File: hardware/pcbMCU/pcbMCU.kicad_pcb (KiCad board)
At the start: 2 copper layers, 53 parts, among them J1 Conn_01x02, J2 Conn_01x04, J3 Conn_01x03, J4 Conn_01x05, SW1 SW_SPDT, U1 AMS1117-3.3, U2 AP62300, U3 STM32L412Cx, U4 Ai-Thinker-Ra-02, U5 RFM95W-915S2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

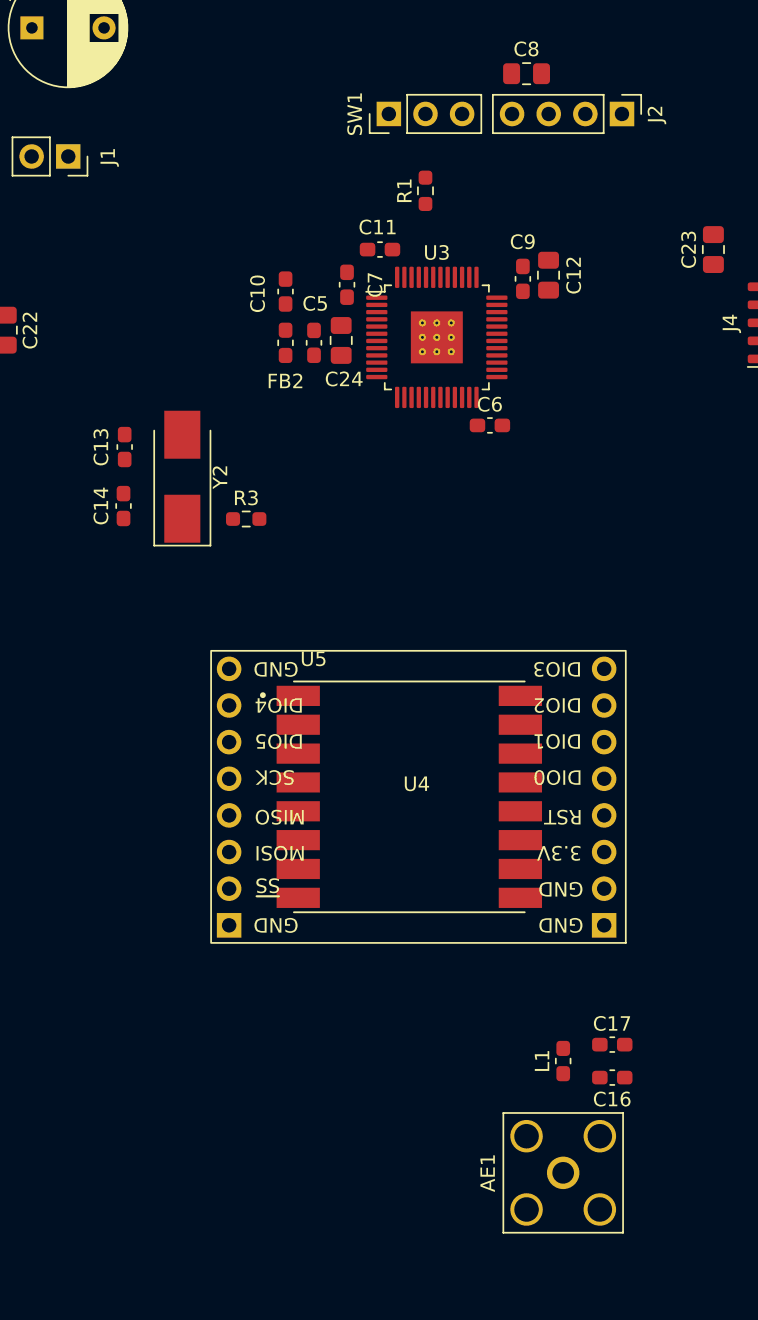
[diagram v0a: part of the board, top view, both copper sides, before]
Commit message: Cambio a ESP32
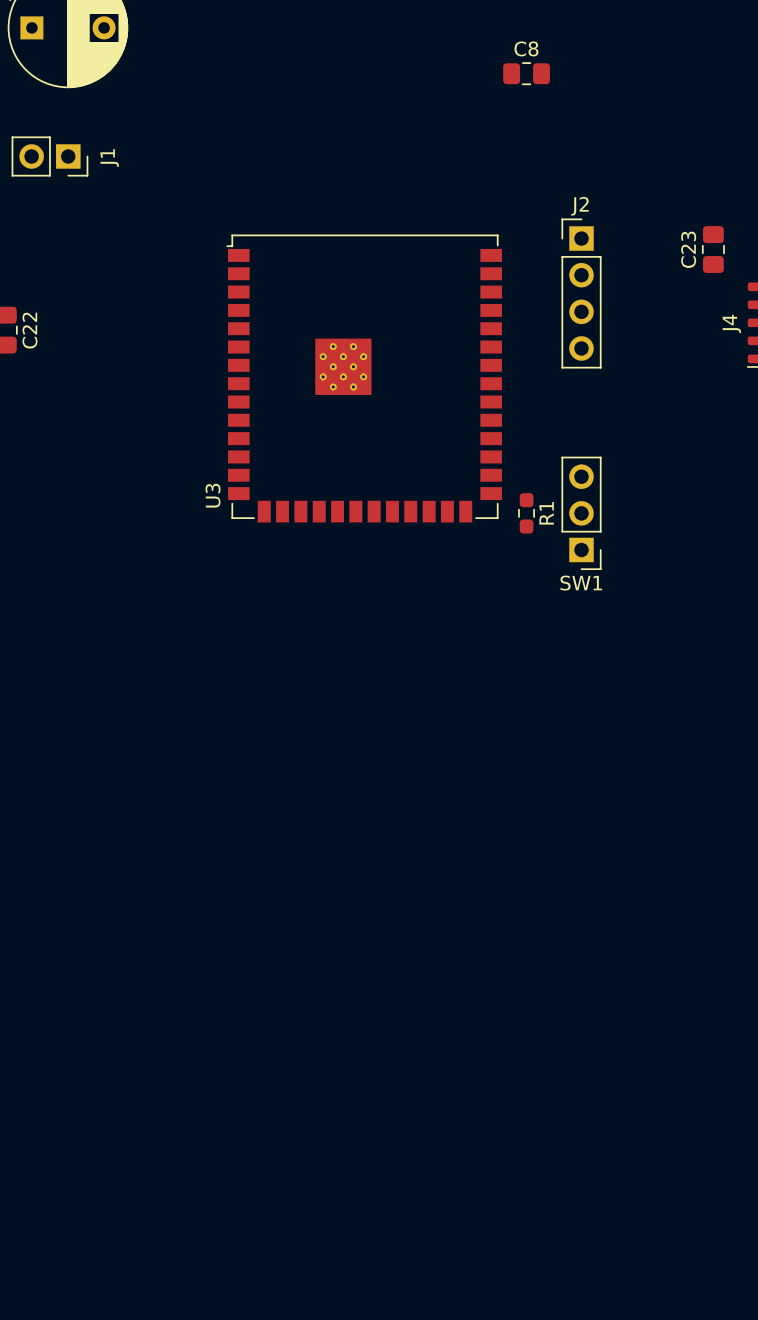
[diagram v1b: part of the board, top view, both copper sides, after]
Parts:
- removed AE1: Antenna_Shield, Connector_Coaxial:SMA_Amphenol_132203-12_Horizontal
- removed C10, C11, C5, C6, C7, C9: 100n, Capacitor_SMD:C_0603_1608Metric_Pad1.08x0.95mm_HandSolder
- removed C12: 4u7, Capacitor_SMD:C_0805_2012Metric_Pad1.18x1.45mm_HandSolder
- removed C13, C14: 10p, Capacitor_SMD:C_0603_1608Metric_Pad1.08x0.95mm_HandSolder
- removed C16, C17: DNP, Capacitor_SMD:C_0603_1608Metric_Pad1.08x0.95mm_HandSolder
- removed C24: 1u, Capacitor_SMD:C_0805_2012Metric_Pad1.18x1.45mm_HandSolder
- removed FB2: 100 @ 100MHz, Inductor_SMD:L_0603_1608Metric_Pad1.05x0.95mm_HandSolder
- removed L1: 0, Inductor_SMD:L_0603_1608Metric_Pad1.05x0.95mm_HandSolder
- removed R3: 0, Resistor_SMD:R_0603_1608Metric_Pad0.98x0.95mm_HandSolder
- removed U4: Ai-Thinker-Ra-02, RF_Module:Ai-Thinker-Ra-02-LoRa-THT
- removed U5: RFM95W-915S2, pcbMCU:XCVR_RFM95W-915S2
- removed Y2: 8MHz, Crystal:Crystal_SMD_0603-2Pin_6.0x3.5mm_HandSoldering
- U3: value STM32L412Cx -> ESP32-S3-WROOM-1; footprint Package_QFP:LQFP-48-1EP_7x7mm_P0.5mm_EP3.6x3.6mm_ThermalVias -> RF_Module:ESP32-S3-WROOM-1U
- moved SW1 33.0 mm to (77.5, 76.2), turned to 180 degrees
- moved R1 23.4 mm to (73.7, 73.7), turned to -90 degrees
- moved J2 9.08 mm to (77.5, 54.6), turned to 0 degrees
- moved U3 5.68 mm to (62.5, 64.2)
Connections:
- net SWDCLK renamed UART_RX
- J2 pad 3: SWDIO -> UART_TX
- U3 pad 1: +3V3 -> GND
- U3 pad 10: ADC_MIC -> unconnected-(U3-Pad10)
- U3 pad 11: ADC_SP -> unconnected-(U3-Pad11)
- U3 pad 15: SPI1_SCK -> unconnected-(U3-Pad15)
- U3 pad 16: SPI1_MISO -> unconnected-(U3-Pad16)
- U3 pad 17: SPI1_MOSI -> unconnected-(U3-Pad17)
- U3 pad 18: ~{SS} -> unconnected-(U3-Pad18)
- U3 pad 19: LoRa_~{RST} -> unconnected-(U3-Pad19)
- U3 pad 2: unconnected-(U3-Pad2) -> +3V3
- U3 pad 20: LoRa_DIO0 -> unconnected-(U3-Pad20)
- U3 pad 23: GND -> unconnected-(U3-Pad23)
- U3 pad 24: +3V3 -> unconnected-(U3-Pad24)
- U3 pad 27: unconnected-(U3-Pad27) -> BOOT0
- U3 pad 3: LS_OSCIN -> unconnected-(U3-Pad3)
- U3 pad 30: SCL_SP -> unconnected-(U3-Pad30)
- U3 pad 31: SDA_SP -> unconnected-(U3-Pad31)
- U3 pad 34: SWDIO -> unconnected-(U3-Pad34)
- U3 pad 35: GND -> unconnected-(U3-Pad35)
- U3 pad 36: +3V3 -> UART_TX
- U3 pad 4: LS_OSCOUT -> unconnected-(U3-Pad4)
- U3 pad 40: unconnected-(U3-Pad40) -> GND
- U3 pad 41: unconnected-(U3-Pad41) -> GND
- U3 pad 5: HS_OSCIN -> unconnected-(U3-Pad5)
- U3 pad 6: HS_OSCOUT -> unconnected-(U3-Pad6)
- U3 pad 7: ~{RST} -> unconnected-(U3-Pad7)
- U3 pad 8: GND -> unconnected-(U3-Pad8)
- U3 pad 9: +3.3VA -> unconnected-(U3-Pad9)

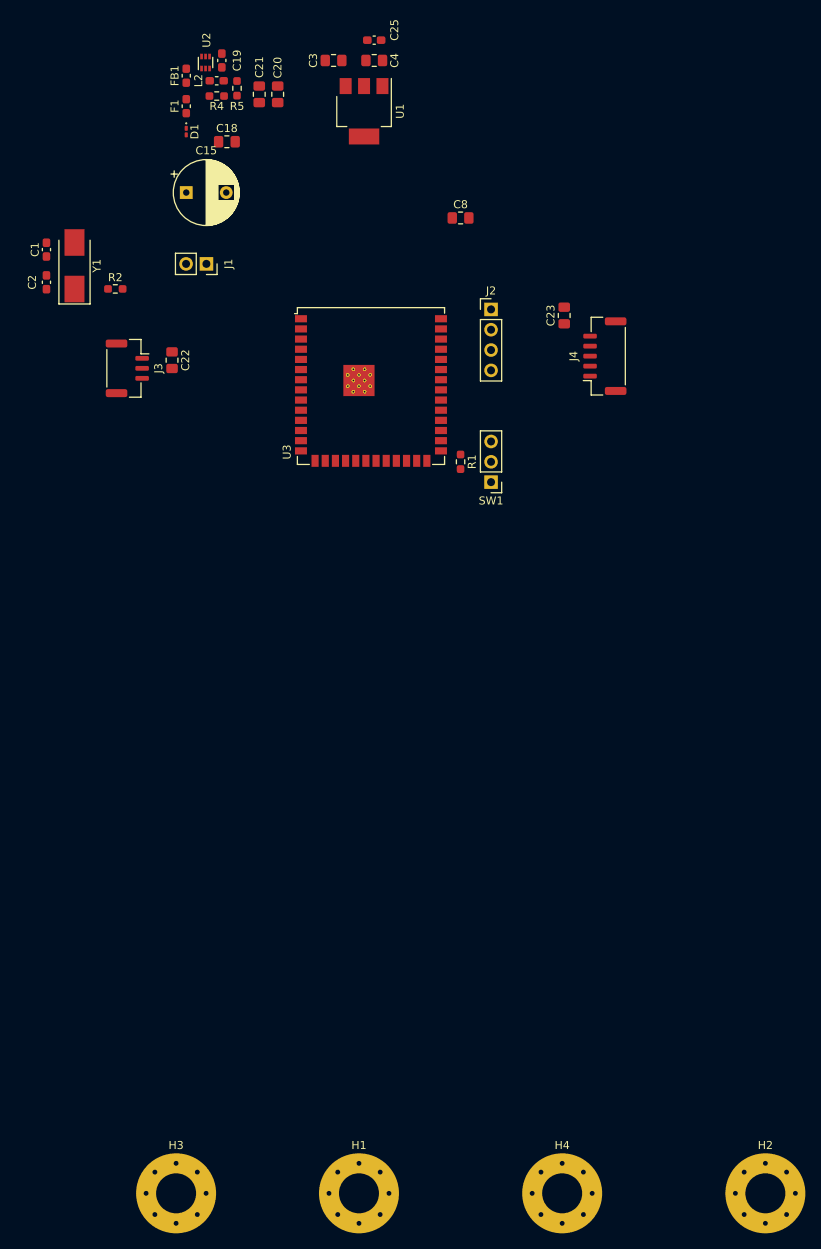
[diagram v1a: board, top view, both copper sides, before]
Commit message: Esquema de PCB inicial, agrupación general de componentes
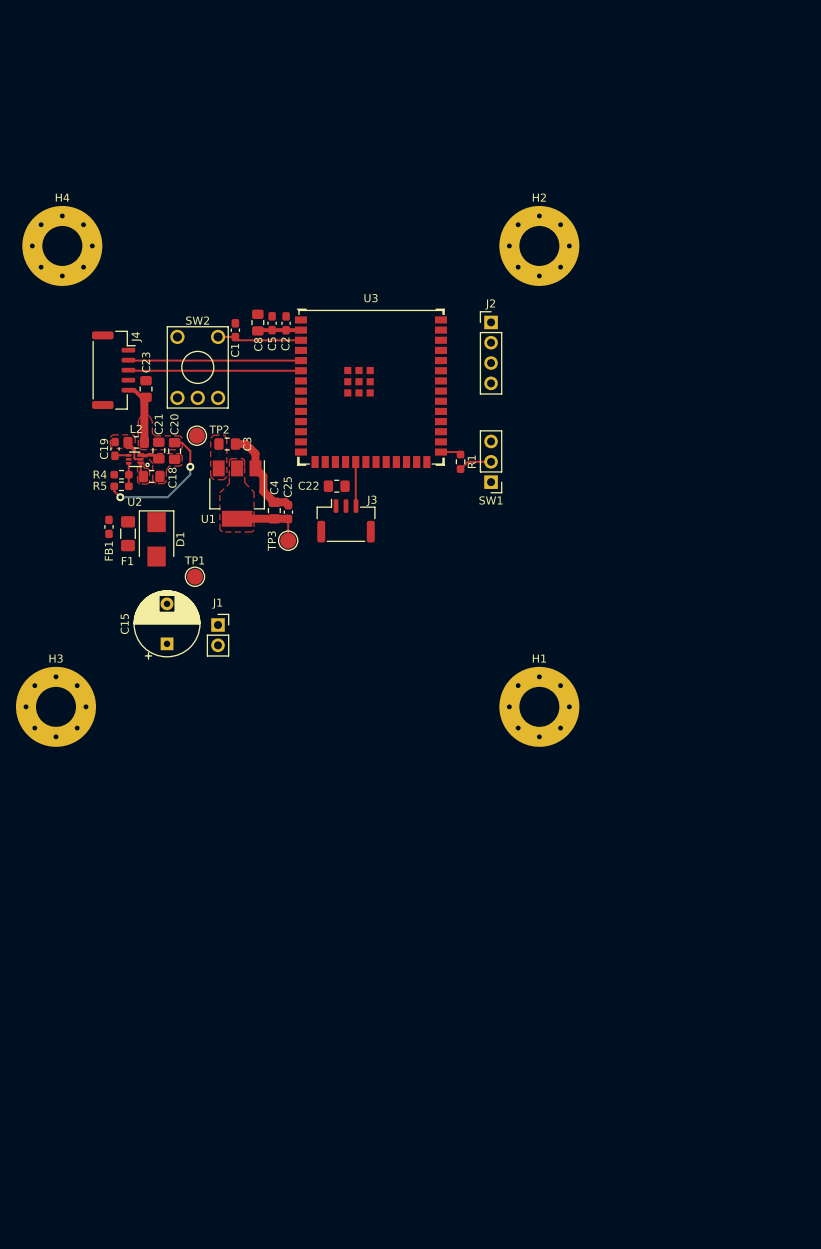
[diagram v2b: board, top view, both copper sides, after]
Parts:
- removed R2: 0, Resistor_SMD:R_0603_1608Metric_Pad0.98x0.95mm_HandSolder
- removed Y1: 32.768 KHz, Crystal:Crystal_SMD_0603-2Pin_6.0x3.5mm_HandSoldering
- added C5: 100n, Capacitor_SMD:C_0603_1608Metric_Pad1.08x0.95mm_HandSolder, F.Cu at (50.1, 56.3)
- added SW2: SW_SPST, Button_Switch_THT:KSA_Tactile_SPST, F.Cu at (38.3, 58.0)
- added TP1: VCC, TestPoint:TestPoint_Pad_D2.0mm, F.Cu at (40.5, 88.0)
- added TP2: 5V, TestPoint:TestPoint_Pad_D2.0mm, F.Cu at (40.7, 70.4)
- added TP3: 3.3V, TestPoint:TestPoint_Pad_D2.0mm, F.Cu at (52.1, 83.5)
- C1: value 10p -> 100n
- C2: value 10p -> 22u
- D1: value D_Schottky_Small -> FM240A; footprint Diode_SMD:D_0201_0603Metric_Pad0.64x0.40mm_HandSolder -> Diode_SMD:D_SMB
- F1: value 500mA -> 1A; footprint Fuse:Fuse_0603_1608Metric_Pad1.05x0.95mm_HandSolder -> Fuse:Fuse_1206_3216Metric_Pad1.42x1.75mm_HandSolder
- L2: footprint Inductor_SMD:L_0603_1608Metric_Pad1.05x0.95mm_HandSolder -> Inductor_SMD:L_0805_2012Metric_Pad1.15x1.40mm_HandSolder
- U3: footprint RF_Module:ESP32-S3-WROOM-1U -> Project Specific:ESP32-S3-WROOM-1U
- moved H4 133.9 mm to (23.9, 46.7)
- moved H2 121.7 mm to (83.5, 46.7)
- moved H1 64.9 mm to (83.5, 104.3)
- moved H3 62.6 mm to (23.1, 104.3)
- moved J4 61.4 mm to (30.3, 62.2), turned to -90 degrees
- moved C25 60.0 mm to (52.1, 80.0), turned to 90 degrees
- moved C4 57.6 mm to (50.4, 79.8), turned to 90 degrees
- moved FB1 57.2 mm to (29.7, 81.8)
- moved C15 56.5 mm to (37.0, 96.4), turned to 90 degrees
- moved F1 53.9 mm to (32.1, 82.7), turned to -90 degrees
- moved C23 53.1 mm to (34.3, 64.6)
- moved R5 51.8 mm to (31.3, 76.7), turned to 180 degrees
- moved D1 51.1 mm to (35.7, 83.3)
- moved U2 50.4 mm to (32.9, 73.3), turned to 180 degrees
- moved C19 50.4 mm to (30.5, 72.1), turned to -90 degrees
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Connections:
- net Net-(C18-Pad1) renamed /BUCK_IN
- net Net-(C19-Pad1) renamed /BUCK_SW
- net Net-(C19-Pad2) renamed /BUCK_BST
- net Net-(R1-Pad2) renamed /BOOT_SW
- net Net-(R4-Pad2) renamed /BUCK_FB
- C1 pad 1: GND -> EN
- C1 pad 2: LS_OSCIN -> GND
- C2 pad 1: GND -> +3V3
- C2 pad 2: Net-(C2-Pad2) -> GND
- U3 pad 19: unconnected-(U3-Pad19) -> ADC_MIC
- U3 pad 3: unconnected-(U3-Pad3) -> EN
- U3 pad 5: unconnected-(U3-Pad5) -> SCL_SP
- U3 pad 6: unconnected-(U3-Pad6) -> SDA_SP
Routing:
- net +5V: track 0.00 -> 25.2 mm, vias 0 -> 2
- net SDA_SP: track 0.00 -> 21.6 mm
- net SCL_SP: track 0.00 -> 21.6 mm
- net +3V3: track 0.00 -> 14.6 mm
- net GND: track 0.00 -> 14.4 mm
- net EN: track 0.00 -> 10.5 mm
- net ADC_MIC: track 0.00 -> 5.51 mm
- net /BOOT_SW: track 0.00 -> 4.19 mm
- net /BUCK_SW: track 0.00 -> 3.16 mm
- net /BUCK_FB: track 0.00 -> 2.88 mm
- net BOOT0: track 0.00 -> 2.58 mm
- net /BUCK_IN: track 0.00 -> 1.78 mm
- net /BUCK_BST: track 0.00 -> 1.74 mm
- added copper zone on F.Cu, net +3V3
- added copper zone on F.Cu, net +5V
- added copper zone on F.Cu, net /BUCK_IN
- added copper zone on F.Cu, net /BUCK_SW
- added copper zone on F.Cu, net GND

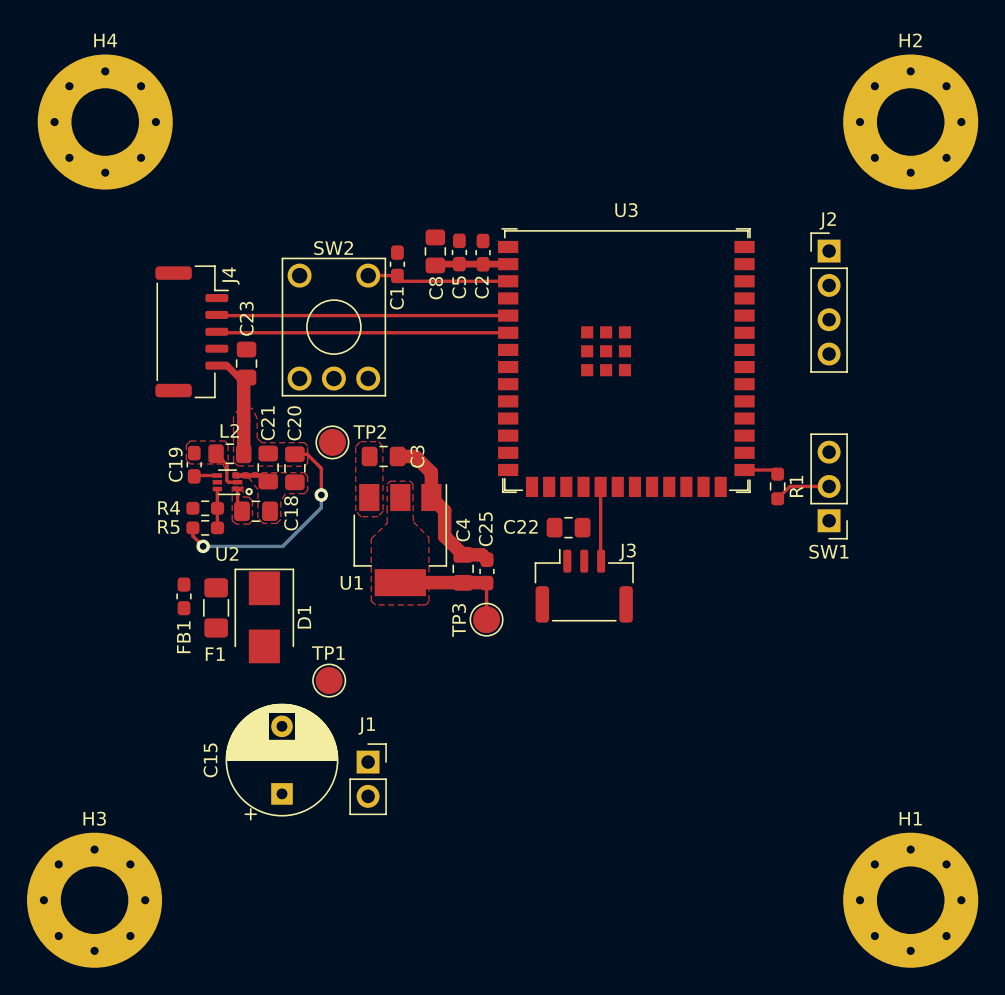
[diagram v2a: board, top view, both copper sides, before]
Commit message: PCB lista para primera revisión
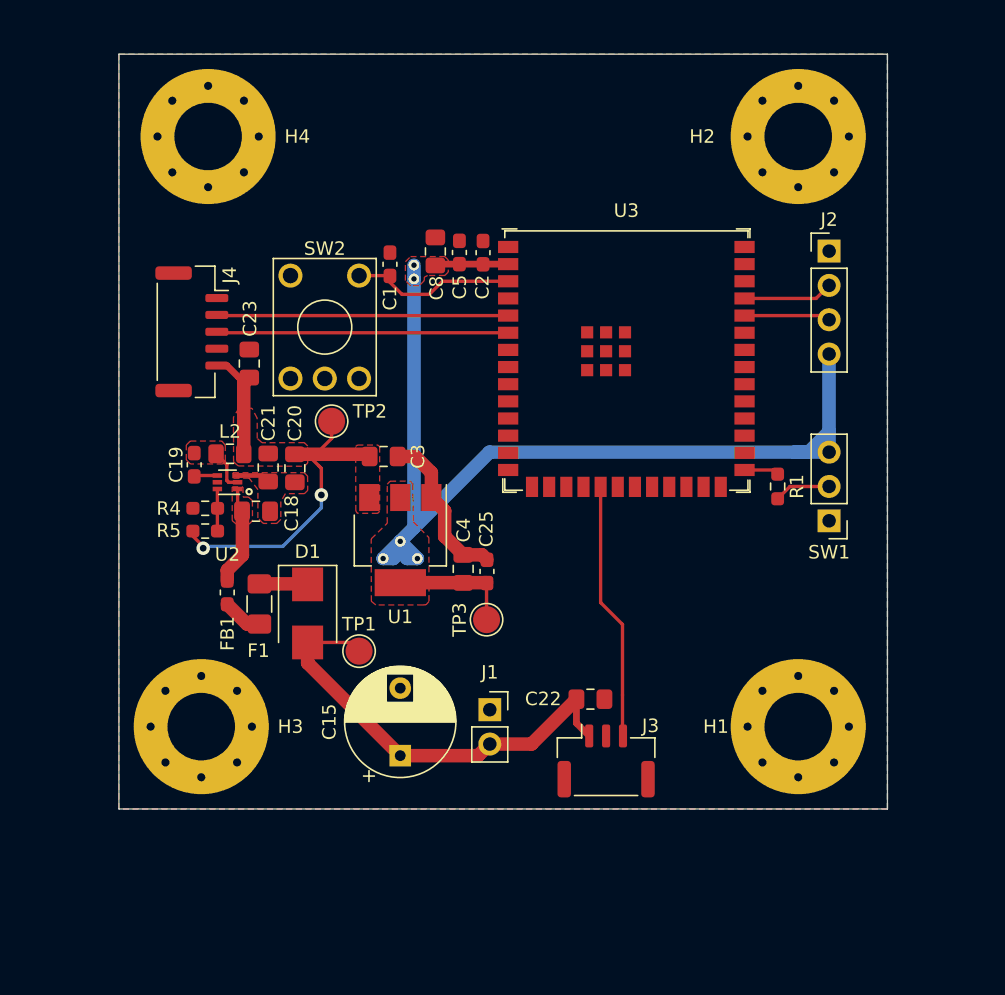
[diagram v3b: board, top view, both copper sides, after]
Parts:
- moved H1 15.3 mm to (75.2, 91.4)
- moved H3 15.1 mm to (31.0, 91.4)
- moved J3 13.0 mm to (61.0, 94.0)
- moved C22 12.8 mm to (59.8, 89.4)
- moved J1 9.81 mm to (52.3, 90.2)
- moved C15 9.20 mm to (45.7, 93.6)
- moved H2 8.39 mm to (75.2, 47.8)
- moved H4 7.69 mm to (31.5, 47.8)
- moved D1 3.22 mm to (38.9, 83.1)
- moved F1 3.22 mm to (35.3, 82.4)
- moved FB1 3.22 mm to (32.9, 81.5)
- moved TP1 3.10 mm to (42.7, 85.9)
- moved TP2 1.57 mm to (40.6, 68.8)
- moved SW2 0.68 mm to (37.6, 58.0)
- moved C1 0.55 mm to (45.0, 57.2)
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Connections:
- H1 pad 1: (no net) -> GND
- H2 pad 1: (no net) -> GND
- H4 pad 1: (no net) -> GND
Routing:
- net +3V3: track 14.6 -> 85.5 mm, vias 0 -> 5
- net VCC: track 0.00 -> 33.2 mm
- net ADC_MIC: track 5.51 -> 19.1 mm
- net +5V: track 25.2 -> 35.7 mm
- net UART_RX: track 0.00 -> 6.66 mm
- net UART_TX: track 0.00 -> 6.39 mm
- net /BUCK_IN: track 1.78 -> 7.40 mm
- net Net-(D1-Pad1): track 0.00 -> 3.59 mm
- net Net-(F1-Pad2): track 0.00 -> 2.99 mm
- net EN: track 10.5 -> 12.3 mm
- added copper zone on B.Cu, net (none)
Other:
- board outline added: 56.9 x 55.9 mm
